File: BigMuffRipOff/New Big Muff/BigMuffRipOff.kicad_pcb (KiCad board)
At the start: 4 copper layers, 50.8 x 84 mm, 92 parts, among them J1 284697-E, J2 NMJ6HFD2, J3 NMJ6HFD2, J4 2125201004, J5 PJ-007, J6 2125201004, J7 2125201004, J8 Conn_01x04, Q1 BC549, Q2 BC549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

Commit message: new big muff completed
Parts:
- removed C16: 0.1u, Capacitor_SMD:C_0603_1608Metric
- removed C27: 10n, Capacitor_SMD:C_0603_1608Metric
- removed C28: 100n, Capacitor_SMD:C_0603_1608Metric
- removed C30: 1u, Capacitor_SMD:C_0603_1608Metric
- removed D1: LED, LED_SMD:LED_0603_1608Metric
- removed the G*** at (148.8, 83.3)
- removed H1, H2, H3, H4: MountingHole, MountingHole:MountingHole_2.2mm_M2
- removed J2, J3: NMJ6HFD2, Connector_Audio:Jack_6.35mm_Neutrik_NMJ6HFD2_Horizontal
- removed J4, J6, J7: 2125201004, 284867-E-footprint:CONN_2125200001-SD_04_MOL
- removed J5: PJ-007, 284867-E-footprint:CONN_PJ-007_SSD
- removed J8: Conn_01x04, Connector_PinHeader_2.54mm:PinHeader_1x04_P2.54mm_Vertical
- removed R30: 270, Resistor_SMD:R_0603_1608Metric
- removed SW3: B3FS-1010P, Button_Switch_SMD:SW_SPST_Omron_B3FS-101xP
- removed U9: STM8L152K4T6, 284867-E-footprint:LQFP-32
- C14: value 10u -> 22u
- C15: value 10u -> 0.47u
- J1: value 284697-E -> Conn_02x08_Odd_Even; footprint 284867-E-footprint:284697E -> Connector_PinHeader_2.54mm:PinHeader_2x08_P2.54mm_Horizontal
- U10: value R-78E3.3-0.5 -> LM2940IMP-9.0/NOPB; footprint Converter_DCDC:Converter_DCDC_RECOM_R-78E-0.5_THT -> GTSR_KiCAD_Footprints:DCY0004A_N
- moved C14 36.0 mm to (163.6, 76.3), turned to -90 degrees
- moved C15 36.0 mm to (173.2, 76.1), turned to -90 degrees
- moved U10 28.2 mm to (168.4, 76.9), turned to -90 degrees
- moved G*** 19.7 mm to (170.6, 99.2), turned to 0 degrees
- moved J1 12.0 mm to (177.5, 78.1), turned to 0 degrees
- moved C20 4.83 mm to (133.6, 80.2), turned to 0 degrees
- moved C19 3.47 mm to (130.8, 75.6), turned to 180 degrees
- moved U6 3.06 mm to (130.0, 78.8)
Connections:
- C15 pad 1: 3.3V -> 12V
- C17 pad 1: /Effect Stage/output_signal -> /GUITAR_OUT
- C18 pad 2: /Effect Stage/input_signal -> /GUITAR_IN
- J1 pad 1: 3.3V -> 12V
- J1 pad 2: /MCU/SWIM -> 12V
- J1 pad 4: /MCU/RST -> GND
- J1 pad 5: GND -> /CS2
- J1 pad 6: GND -> /SPI_CLK
- J1 pad 7: GND -> /CS1
- J1 pad 8: GND -> /GUITAR_IN
- R1 pad 1: /Effect Stage/input_signal -> /GUITAR_IN
- U1 pad 4: /Effect Stage/SPI_CLK -> /SPI_CLK
- U1 pad 5: /Effect Stage/SPI_MOSI -> /MOSI
- U1 pad 6: /Effect Stage/CS_1 -> /CS2
- U10 pad 1: 9V -> 12V
- U10 pad 3: 3.3V -> 9V
- U2 pad 4: /Effect Stage/SPI_CLK -> /SPI_CLK
- U2 pad 5: /Effect Stage/SPI_MOSI -> /MOSI
- U2 pad 6: /Effect Stage/CS_2 -> /CS1
- U3 pad 4: /Effect Stage/SPI_CLK -> /SPI_CLK
- U3 pad 5: /Effect Stage/SPI_MOSI -> /MOSI
- U3 pad 6: /Effect Stage/CS_4 -> /CS3
- U8 pad 4: /Effect Stage/SPI_CLK -> /SPI_CLK
- U8 pad 5: /Effect Stage/SPI_MOSI -> /MOSI
- U8 pad 6: /Effect Stage/CS_3 -> /CS0
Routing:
- net /MOSI: track 0.00 -> 114.8 mm, vias 0 -> 5
- net /SPI_CLK: track 0.00 -> 111.6 mm, vias 0 -> 5
- net /Effect Stage/SPI_MOSI: track 86.5 -> 0.00 mm, vias 4 -> 0
- net /Effect Stage/SPI_CLK: track 80.1 -> 0.00 mm, vias 8 -> 0
- net /GUITAR_IN: track 0.00 -> 62.6 mm
- net /CS2: track 0.00 -> 54.6 mm, vias 0 -> 1
- net /CS3: track 0.00 -> 46.4 mm, vias 0 -> 1
- net /MCU/RST: track 38.9 -> 0.00 mm, vias 2 -> 0
- net /Effect Stage/CS_3: track 31.3 -> 0.00 mm, vias 2 -> 0
- net /Effect Stage/CS_4: track 30.0 -> 0.00 mm, vias 2 -> 0
- net /Effect Stage/input_signal: track 28.2 -> 0.00 mm
- net /Effect Stage/CS_1: track 28.1 -> 0.00 mm, vias 2 -> 0
- net /GUITAR_OUT: track 0.00 -> 25.6 mm, vias 0 -> 2
- net /MCU/Pot_3: track 23.4 -> 0.00 mm
- net /Effect Stage/CS_2: track 19.1 -> 0.00 mm, vias 2 -> 0
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- added copper zone on F.Cu, net 12V
- added copper zone on F.Cu, net 9V
- removed copper zone on In2.Cu, net 3.3V
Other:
- board size 50.8 x 84 mm -> 59.3 x 32 mm
- board text added: "BigMuff RipOff Rev 1.0 Marco Yaipen March 9, 2026"
- board text removed: "Marco Yaipen BigMuff RipOff Rev 1.0 February 14, 2026"

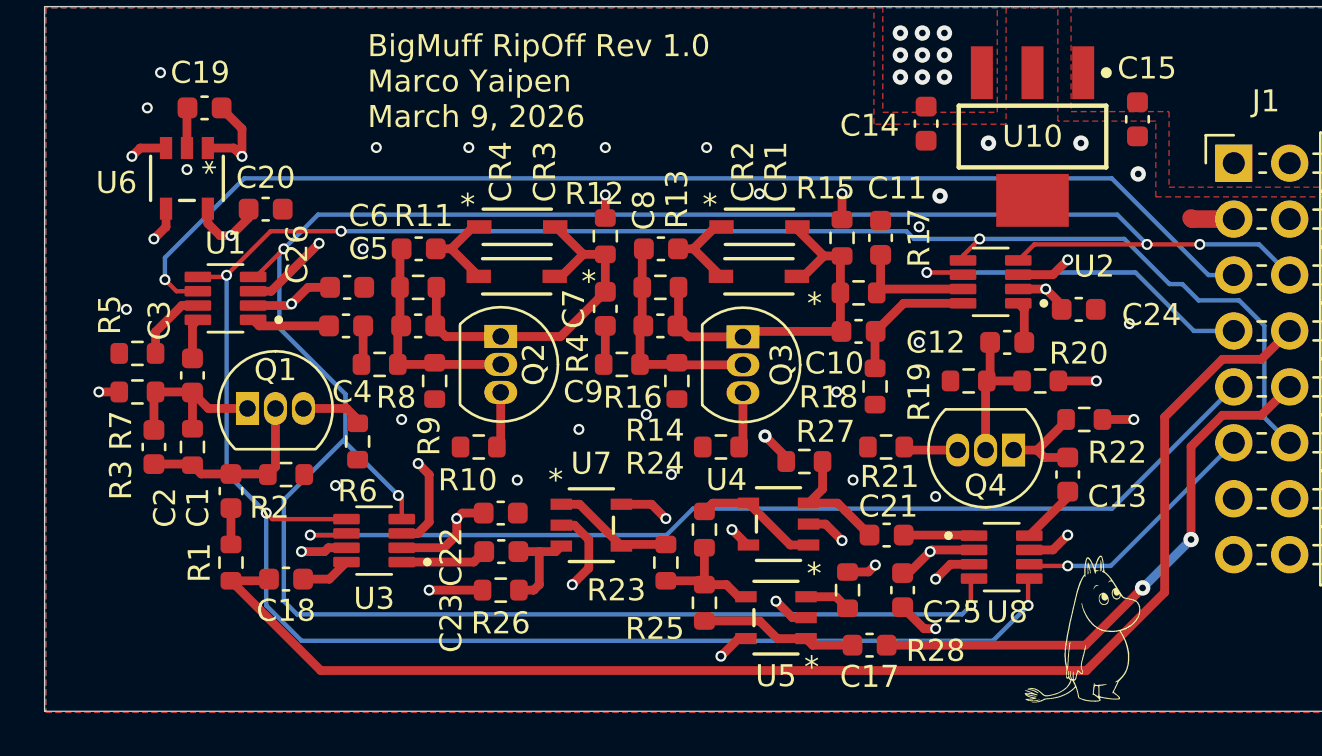
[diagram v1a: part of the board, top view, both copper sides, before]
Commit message: removed the old diodes from before
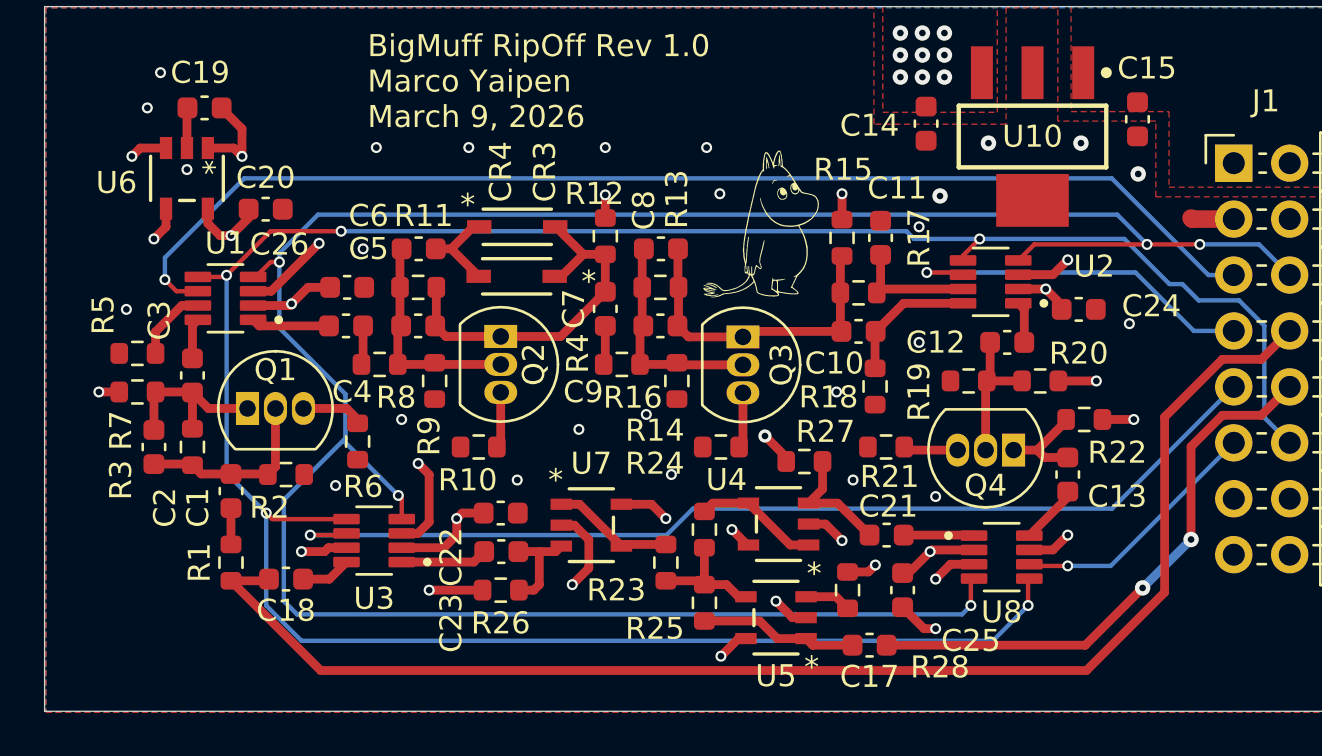
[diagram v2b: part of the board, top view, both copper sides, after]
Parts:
- removed CR1, CR2: 1N4148W-13-F, 284867-E-footprint:SOD123_DIO
- moved G*** 23.5 mm to (156.0, 80.8)
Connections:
- C8 pad 1: Net-(C8-Pad1) -> Net-(Q3-C)
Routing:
- net Net-(C8-Pad1): track 4.16 -> 0.00 mm
- net Net-(Q3-C): track 17.3 -> 14.8 mm
